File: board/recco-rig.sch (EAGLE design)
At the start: 34 parts, among them IC1 LM386, IC2 TL072-OPAMP, P10-LINE-IN PIN-HEADER-2PIN, P2-SPKR-OUT PIN-HEADER-3PIN, P3-SPKR-MIC-IN PIN-HEADER-4PIN

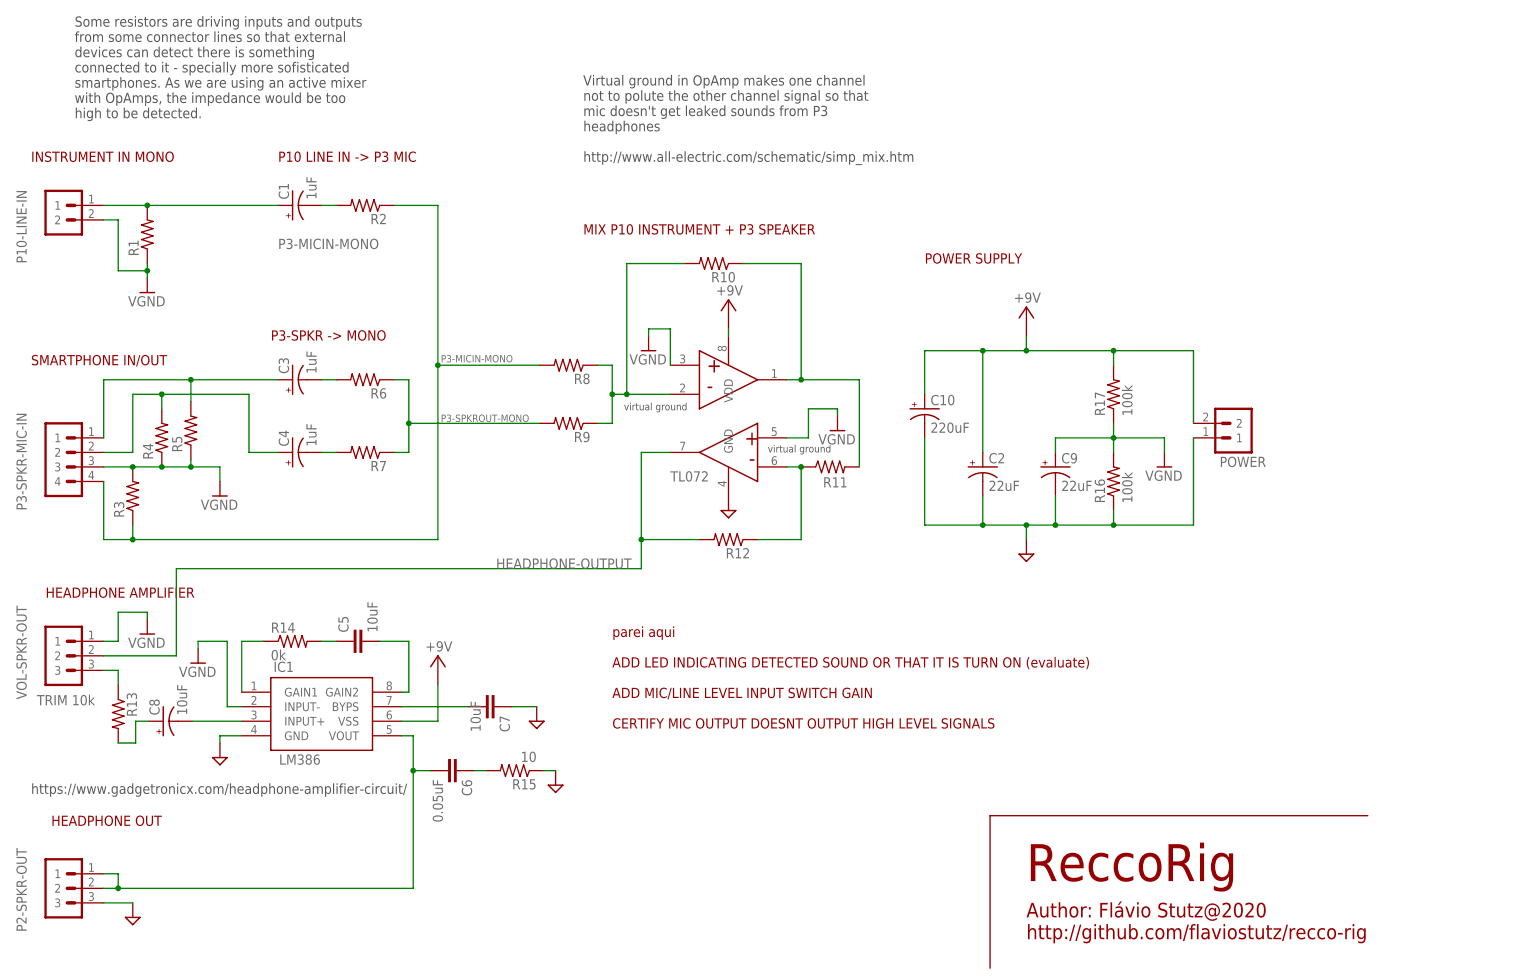
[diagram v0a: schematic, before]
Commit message: physical board and mic protection
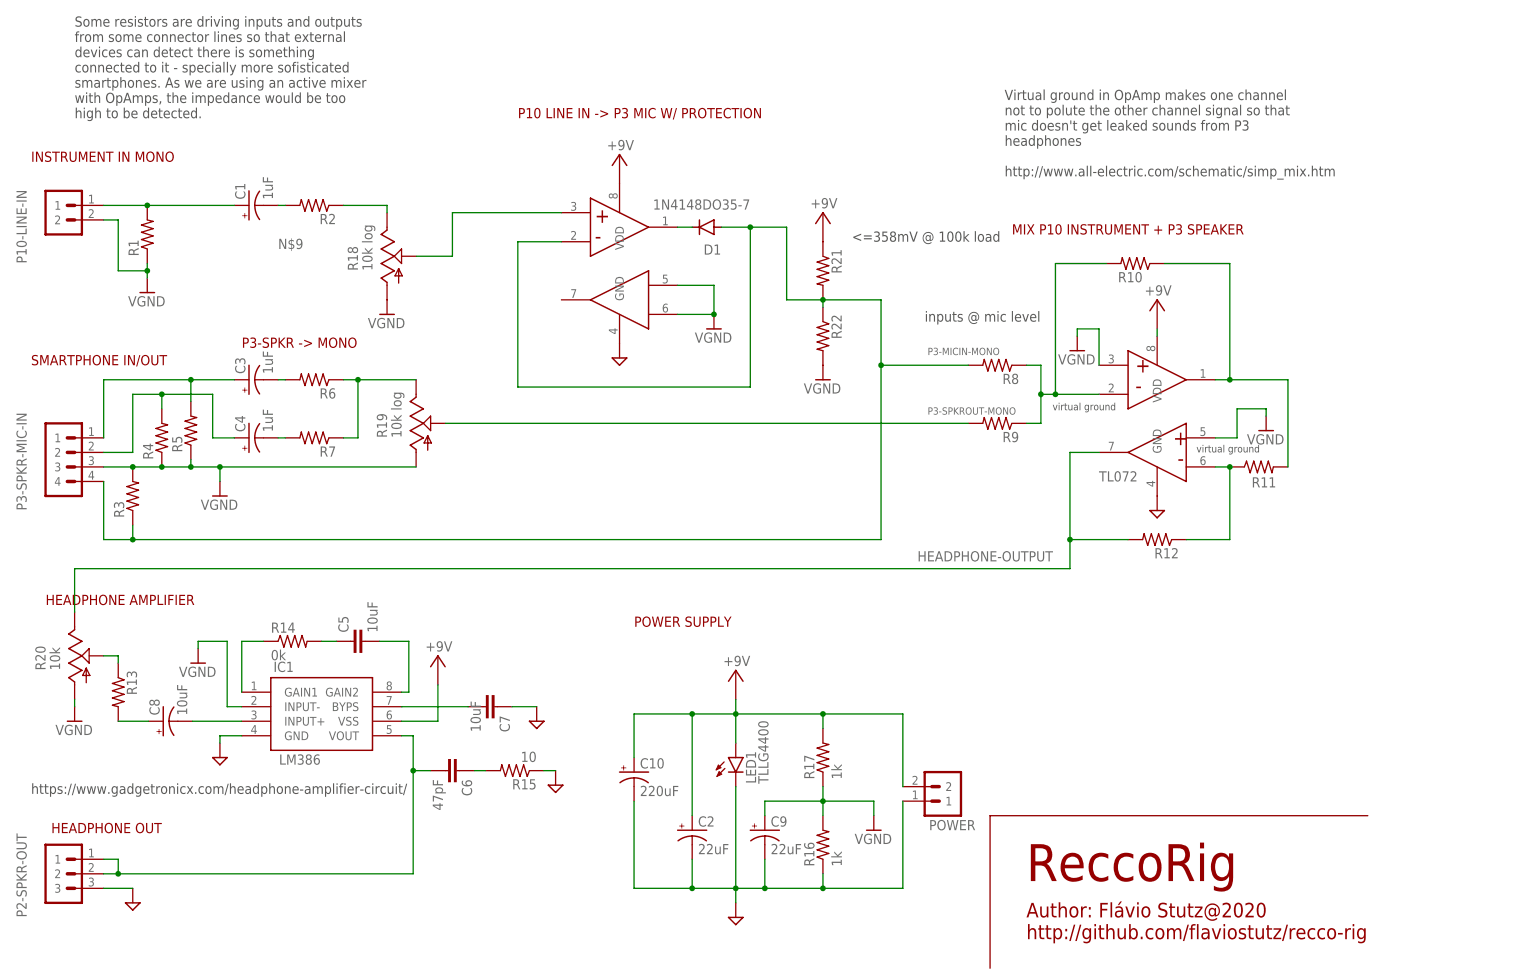
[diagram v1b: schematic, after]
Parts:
- removed VOL-SPKR-OUT: HEADPHONE-VOLUME-KNOB, stutz-components-library:PIN-HEADER-3PIN
- added D1: 1N4148DO35-7, diode:1N4148DO35-7
- added LED1: TLLG4400, led:TLLG4400
- added R18, R19: 10k log, pot:TRIM_US-B25U
- added R20: 10k, pot:TRIM_US-B25U
- added R21: 10k, stutz-components-library:RESISTORV1
- added R22: 1k, stutz-components-library:RESISTORV1
- added U$12: TL072-OPAMP, stutz-components-library:TL072-OPAMP
- C6: value 0.05uF -> 47pF
- R16, R17: value 100k -> 1k
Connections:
- new net N$18: R19.E, R6.1, R7.1
- new net N$19: R18.S, U$12.1IN+
- new net N$21: D1.C, U$12.1OUT
- new net N$9: R18.E, R2.1
- net +9V: now also LED1.A, R21.1, U$12.VDD
- net GND: now also LED1.C, U$12.GND
- net HEADPHONE-OUTPUT: now also R20.E; no longer VOL-SPKR-OUT.2
- net N$11: now also R20.S; no longer VOL-SPKR-OUT.3
- net P3-MICIN-MONO: now also D1.A, R21.2, R22.1, U$12.1IN-; no longer R2.1
- net P3-SPKROUT-MONO: now also R19.S; no longer R6.1, R7.1
- net VGND: now also R18.A, R19.A, R20.A, R22.2, U$12.2IN+, U$12.2IN-; no longer VOL-SPKR-OUT.1
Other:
- note added: "<=358mV @ 100k load"
- note added: "P10 LINE IN -> P3 MIC W/ PROTECTION"
- note added: "inputs @ mic level"
- note removed: "P10 LINE IN -> P3 MIC"
- note removed: "TRIM 10k"
- note removed: "parei aqui ADD LED INDICATING DETECTED SOUND OR THAT IT IS TURN ON (evaluate) ADD MIC/LINE LEVEL INPUT SWITCH GAIN CERTIFY MIC OUTPUT DOESNT OUTPUT HIGH LEVEL SIGNALS"
- moved on the sheet: C1, C10, C2, C3, C4, C9, P2-SPKR-OUT, POWER, R10, R11, R12, R13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
